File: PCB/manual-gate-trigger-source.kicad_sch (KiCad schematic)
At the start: 60 parts

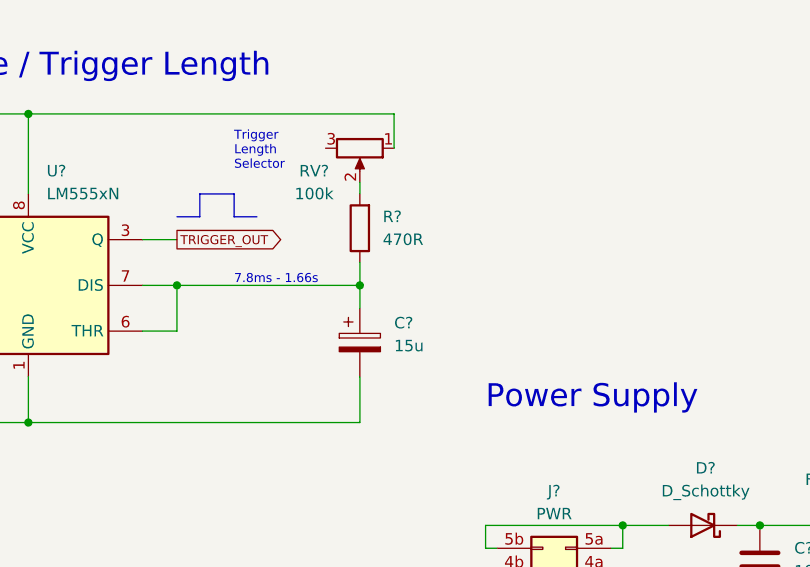
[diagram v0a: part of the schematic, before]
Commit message: :hammer: Adjust RC element of 555 gate length generator
according to
https://github.com/moPsy-project/manual-gate-trigger-source/issues/9#issuecomment-1377659194
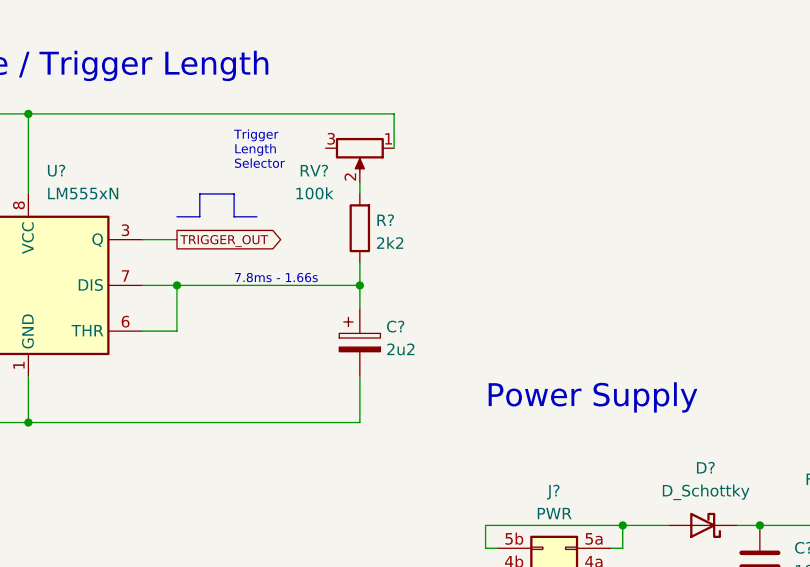
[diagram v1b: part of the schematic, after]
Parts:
- C?: value 15u -> 2u2
- R?: value 470R -> 2k2
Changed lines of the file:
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@@
   (symbol (lib_id "Device:C_Polarized") (at 153.67 110.49 0) (unit 1)
     (in_bom yes) (on_board yes) (fields_autoplaced)
-    (property "Reference" "C?" (id 0) (at 157.48 108.3309 0)
-      (effects (font (size 1.27 1.27)) (justify left))
-    )
-    (property "Value" "15u" (id 1) (at 157.48 110.8709 0)
+    (property "Reference" "C?" (id 0) (at 156.591 108.7663 0)
+      (effects (font (size 1.27 1.27)) (justify left))
+    )
+    (property "Value" "2u2" (id 1) (at 156.591 111.3032 0)
       (effects (font (size 1.27 1.27)) (justify left))
     )
@@
   (symbol (lib_id "Device:R") (at 153.67 97.79 180) (unit 1)
     (in_bom yes) (on_board yes) (fields_autoplaced)
-    (property "Reference" "R?" (id 0) (at 156.21 96.5199 0)
-      (effects (font (size 1.27 1.27)) (justify right))
-    )
-    (property "Value" "470R" (id 1) (at 156.21 99.0599 0)
+    (property "Reference" "R?" (id 0) (at 155.448 96.9553 0)
+      (effects (font (size 1.27 1.27)) (justify right))
+    )
+    (property "Value" "2k2" (id 1) (at 155.448 99.4922 0)
       (effects (font (size 1.27 1.27)) (justify right))
     )
@@
     )
     (path "/90788551-bdc4-4dcd-9cb8-fffcee0cf080"
-      (reference "C?") (unit 1) (value "15u") (footprint "")
+      (reference "C?") (unit 1) (value "2u2") (footprint "")
     )
     (path "/90dff1fa-7a83-4bb0-9dd9-0464957e6caa"
@@
     )
     (path "/9b1418bd-cfcd-4c7b-a3f1-f1dc5c5b0f85"
-      (reference "R?") (unit 1) (value "470R") (footprint "")
+      (reference "R?") (unit 1) (value "2k2") (footprint "")
     )
     (path "/9bc9eafd-e631-4665-9711-575db6e1ad61"

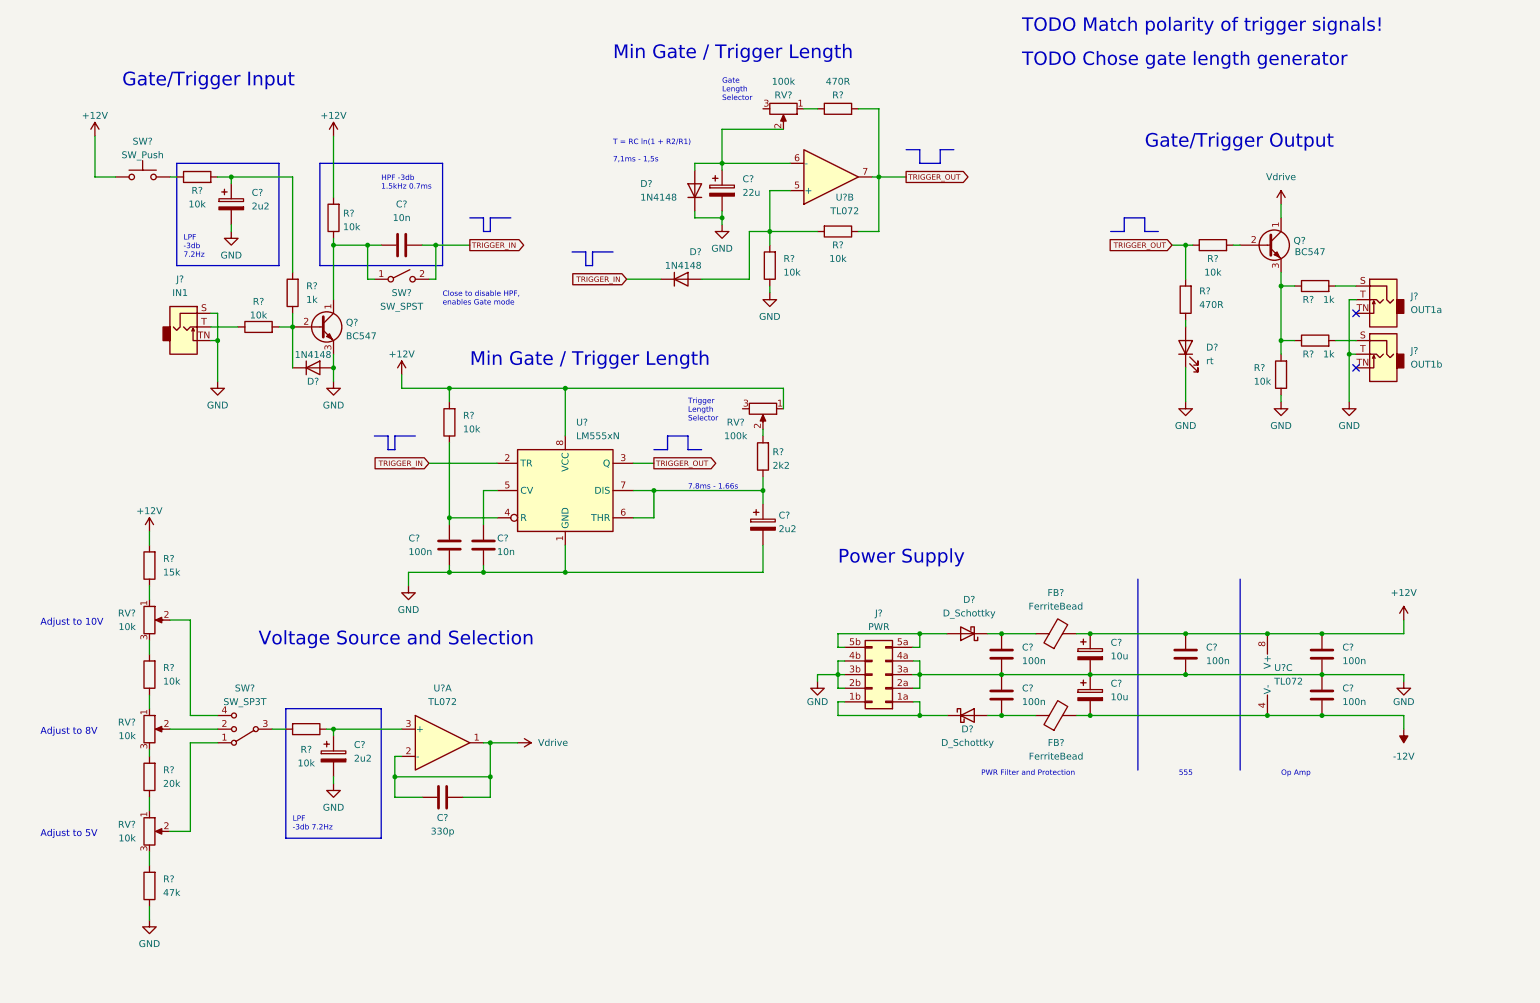
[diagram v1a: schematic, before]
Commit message: :fire: Remove the op-amp design for gate length generator
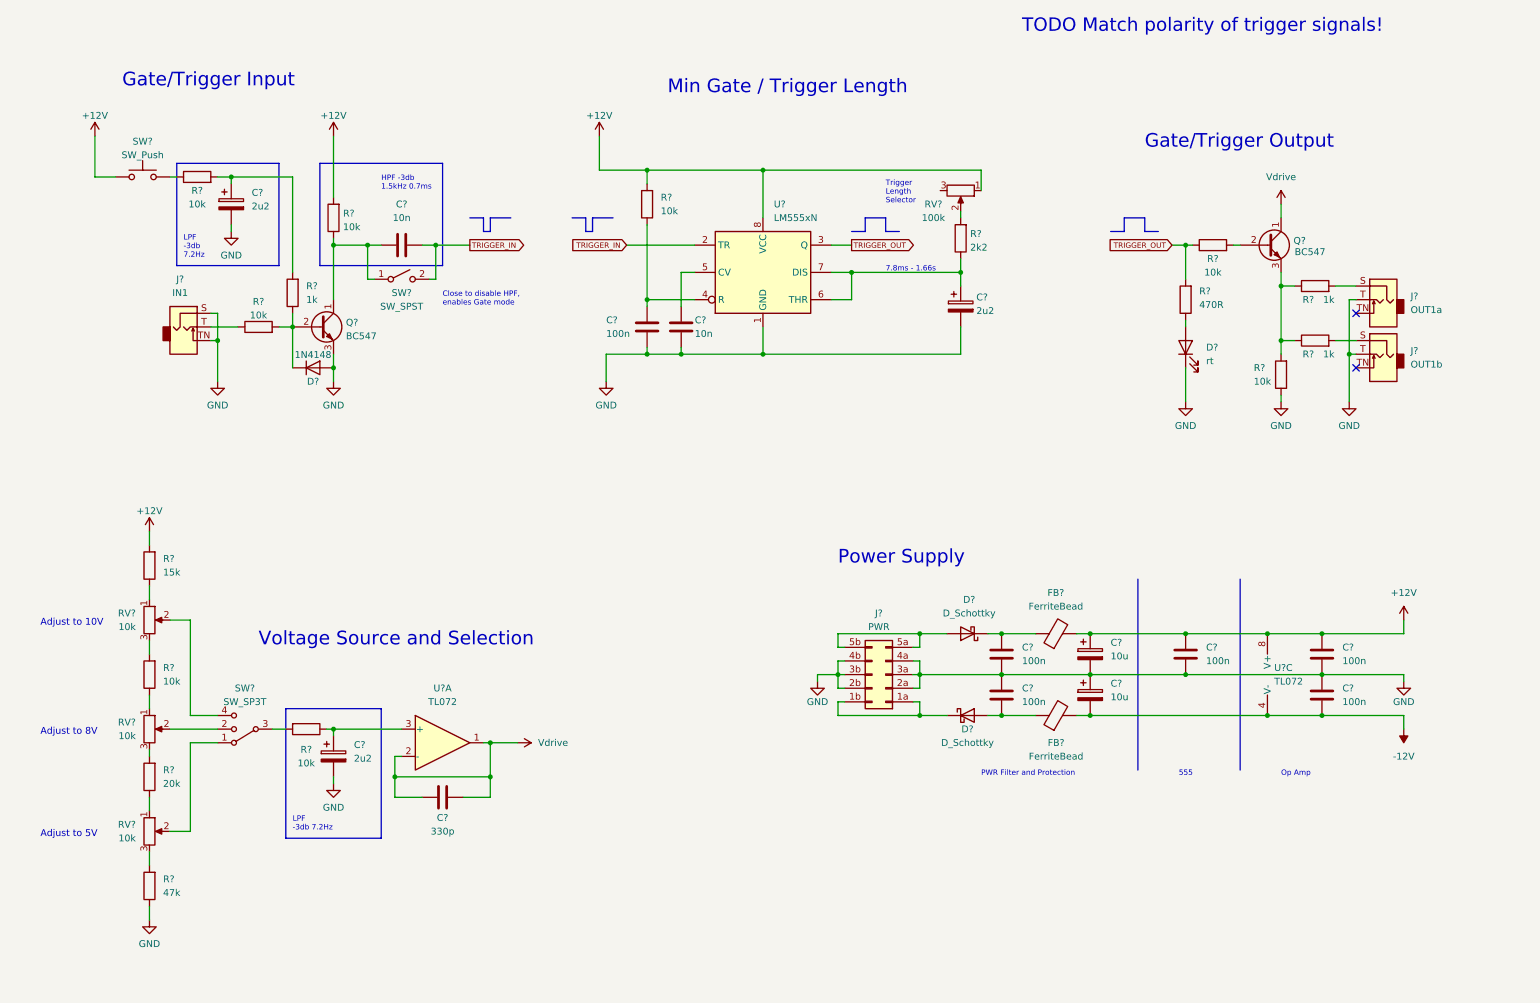
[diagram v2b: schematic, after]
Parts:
- removed C?: 22u, symbol Device:C_Polarized
- removed D? (x2): 1N4148, symbol Device:D
- removed R?: 470R, symbol Device:R
- removed R? (x2): 10k, symbol Device:R
- removed RV?: 100k, symbol Device:R_Potentiometer
- removed U?: TL072, symbol Amplifier_Operational:TL072
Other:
- note removed: "Gate Length Selector"
- note removed: "T = RC ln(1 + R2/R1) 7,1ms - 1,5s"
- note removed: "TODO Chose gate length generator"
- moved on the sheet: C?, R?, RV?, U?

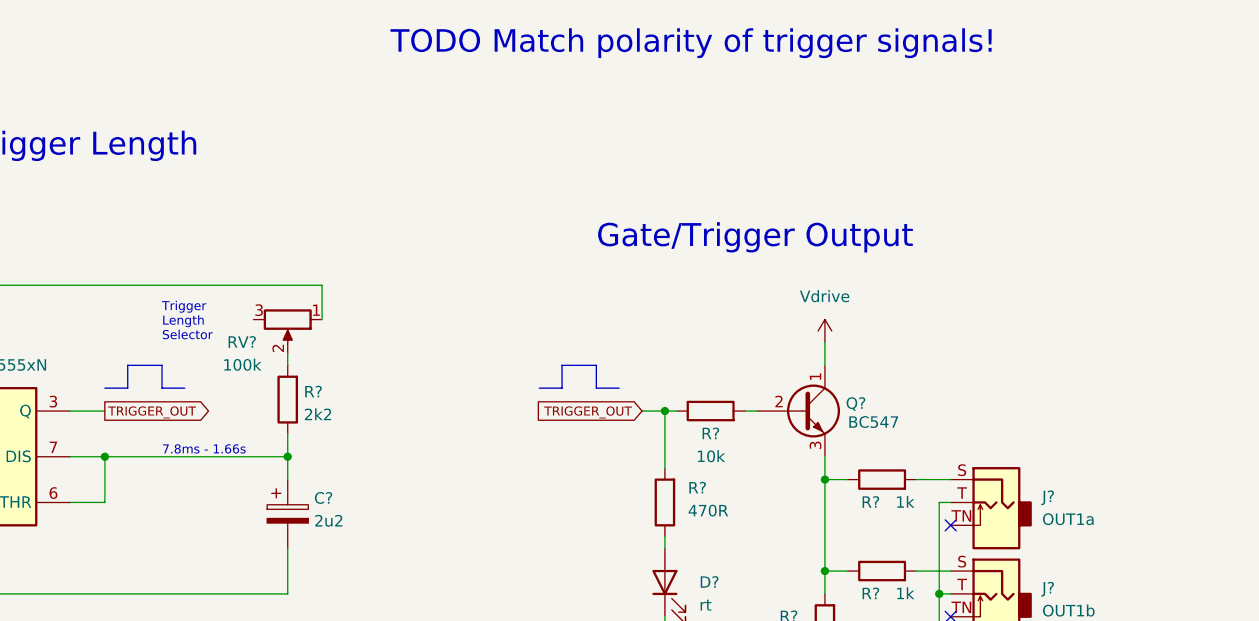
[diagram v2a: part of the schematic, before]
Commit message: :memo: Remove todo and fix RC annotation
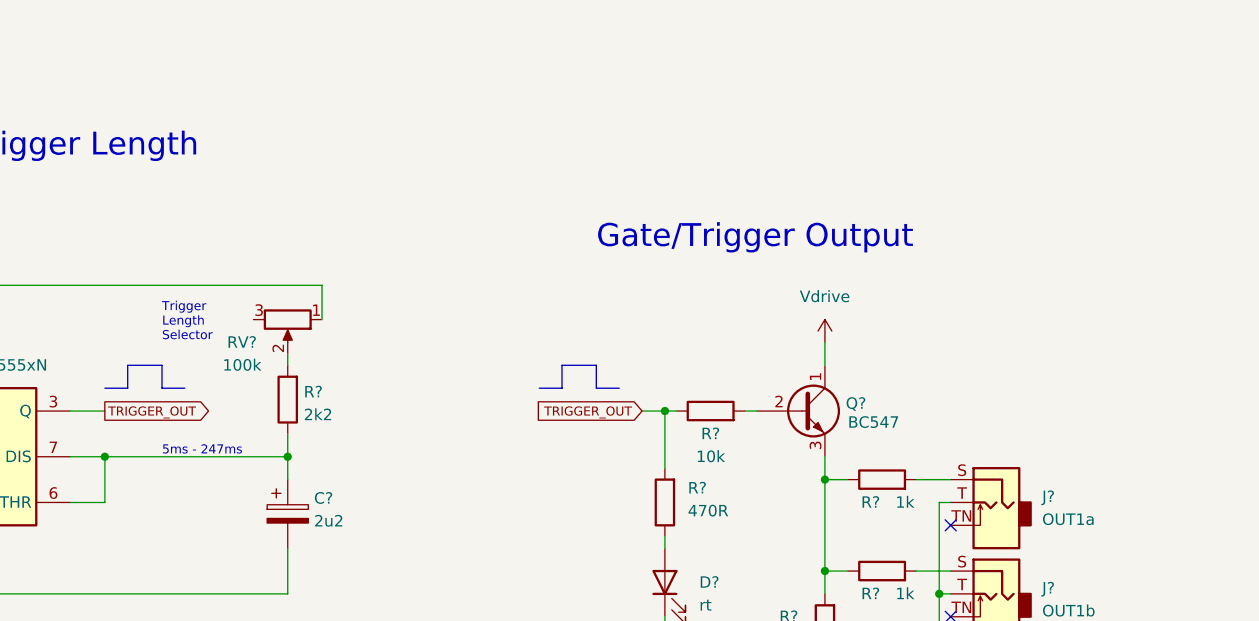
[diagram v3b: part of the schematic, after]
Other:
- note added: "5ms - 247ms"
- note removed: "7.8ms - 1.66s"
- note removed: "TODO Match polarity of trigger signals!"
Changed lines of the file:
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@@
     (effects (font (size 1 1)) (justify left bottom))
-  )
-  (text "TODO Match polarity of trigger signals!" (at 201.93 19.05 0)
-    (effects (font (size 2.5 2.5)) (justify left bottom))
   )
   (text "Voltage Source and Selection" (at 59.69 133.35 0)
@@
     (effects (font (size 1.27 1.27)) (justify left bottom))
   )
-  (text "7.8ms - 1.66s" (at 176.53 63.5 0)
+  (text "5ms - 247ms" (at 176.53 63.5 0)
     (effects (font (size 1 1)) (justify left bottom))
   )
